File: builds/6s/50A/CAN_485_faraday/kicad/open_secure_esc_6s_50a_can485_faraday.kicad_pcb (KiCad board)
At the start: 4 copper layers, 32 x 66.1 mm, 59 parts, among them J1 SolderPad_1x04_SMD_P1.27mm_Pr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, J2 SolderPad_1x02_SMD_P2.54mm, J3 SolderPad_1x02_SMD_P2.54mm, J4A SolderWirePad_1x01_SMD_5x10mm, J4B SolderWirePad_1x01_SMD_5x10mm, J4C SolderWirePad_1x01_SMD_5x10mm, J5A SolderWire-6sqmm_1x01_D3.5mm_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, J5B SolderWire-6sqmm_1x01_D3.5mm_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, Q1 Toshiba_2-5W1A_SOP-Advance-N_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, Q2 Toshiba_2-5W1A_SOP-Advance-N_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, Q3 Toshiba_2-5W1A_SOP-Advance-N_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, Q4 Toshiba_2-5W1A_SOP-Advance-N_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, Q5 Toshiba_2-5W1A_SOP-Advance-N_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, Q6 Toshiba_2-5W1A_SOP-Advance-N_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, U1 LQFP-64_10x10mm_P0.5mm, U2 Infineon_PG-USON-10-2-4_3x3mm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, U3 SOIC-20W_7.5x12.8mm_P1.27mm, U4 SOIC-20W_7.5x12.8mm_P1.27mm, U5 TI_RTA0040B_WQFN-40_6x6mm_P0.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, U6 SOIC-8_3.9x4.9mm_P1.27mm, U7 SOIC-8_3.9x4.9mm_P1.27mm, U8 SOIC-8_3.9x4.9mm_P1.27mm

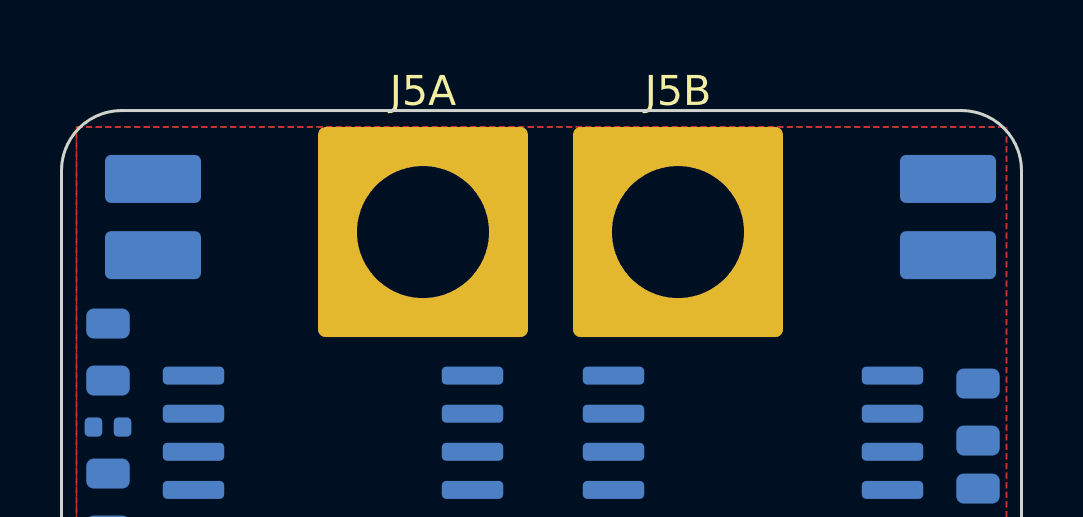
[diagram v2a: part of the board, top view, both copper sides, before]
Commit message: Check the PCB skills for IPC-2152: neither has it, and one misattributes 2221
The repo owner pointed at pcb-engineer and pcb-designer as holding IPC-2152
reference tables. Read both. Neither does.

pcb-engineer/references/design-rules.md prints

    Area = (I / (k x dT^0.44))^(1/0.725),  k = 0.048 external / 0.024 internal

under the heading "the IPC-2152 formula". Those are IPC-2221 Appendix A
constants, inherited from IPC-D-275. IPC-2152 replaced those curves BECAUSE
they were found inaccurate, and it publishes charts rather than a closed-form
k/b/c. conductor_sizing.py already recorded this in August; this run
quantifies it.

The document also disagrees with itself, and the error grows with current:

     I (A)   its table   its formula   ratio
       0.5        0.13          0.12   1.13x
       1.0        0.38          0.30   1.27x
       5.0        5.00          2.77   1.81x
      10.0       16.00          7.19   2.22x

This build runs at 50 A -- five times past that table's last row, in the
direction where its self-disagreement is worst.

pcb-designer carries no 2152 chart data at all; its trace table ends at
"Power >1A -> copper pour" and is silent at this current. Neither reference
carries a wire ampacity or AWG table, so neither speaks to the pack-lead
sizing flagged UNVERIFIED earlier -- IPC-2152 governs PCB conductors, not
wires, so it would not have anyway.

WHAT RUNNING IT ANYWAY REVEALS, recorded as information not citation: that
2221 equation asks for 14.28 mm (40 C rise) to 33.12 mm (10 C rise) of
external 2 oz conductor at 50 A. This build's phase pours are 7.50 mm -- two
to four times narrower.

That is not proof they are wrong. The equation models an isolated trace in
still air; these pours are 2.93 squares, wide, and pressed against the In1/In2
planes, and [47] measures a shipping 6S/50 A ESC at 103 C on a smaller board.
But it sizes the gap this design carries on unquantified plane spreading, and
it is precisely what IPC-2152's charts exist to s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
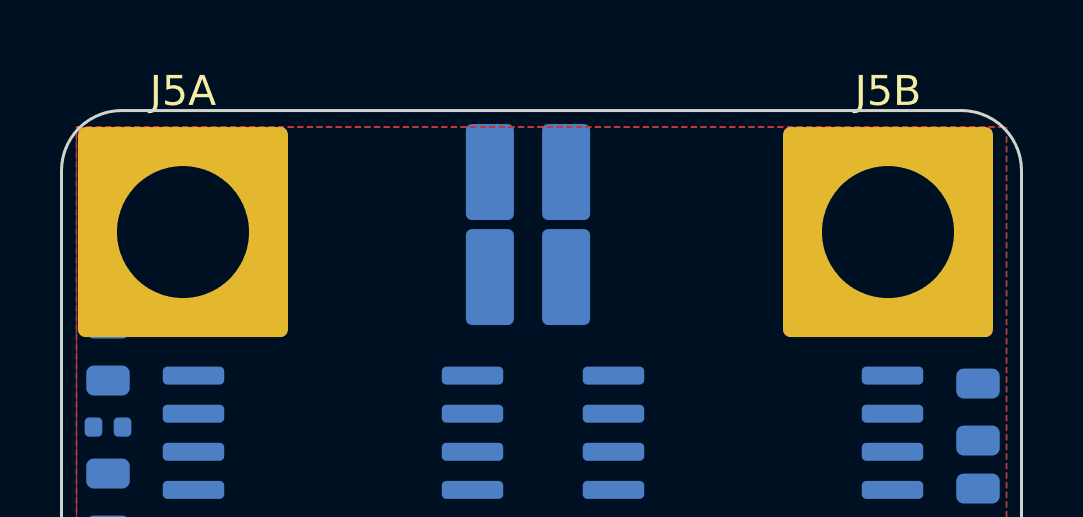
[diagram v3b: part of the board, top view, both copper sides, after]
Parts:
- moved J3 14.1 mm to (35.5, 25.5), turned to 180 degrees
- moved J2 12.6 mm to (35.5, 22.0), turned to 0 degrees
- moved J5A 8.00 mm to (24.0, 24.0)
- moved J5B 7.00 mm to (47.5, 24.0)
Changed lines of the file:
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@@
 	(footprint "SolderWire-6sqmm_1x01_D3.5mm_OD7mm"
 		(layer "F.Cu")
-		(at 32 24)
+		(at 24 24)
 		(descr "Soldered wire connection, for a single 6 mm² wire, reinforced insulation, conductor diameter 3.5mm, outer diameter 7mm, size source Multi-Contact FLEXI-xV 2.5 (https://www.staubli.com/content/dam/ecs/catalogs-brochures/TM/CAB-Main-11014119-en.pdf#page=11), bend radius 3 times outer diameter, generated with kicad-footprint-generator")
 		(tags "connector wire 6sqmm")
@@
 	(footprint "SolderWire-6sqmm_1x01_D3.5mm_OD7mm"
 		(layer "F.Cu")
-		(at 40.5 24)
+		(at 47.5 24)
 		(descr "Soldered wire connection, for a single 6 mm² wire, reinforced insulation, conductor diameter 3.5mm, outer diameter 7mm, size source Multi-Contact FLEXI-xV 2.5 (https://www.staubli.com/content/dam/ecs/catalogs-brochures/TM/CAB-Main-11014119-en.pdf#page=11), bend radius 3 times outer diameter, generated with kicad-footprint-generator")
 		(tags "connector wire 6sqmm")
@@
 	(footprint "SolderPad_1x02_SMD_P2.54mm"
 		(layer "B.Cu")
-		(at 23 23.5 90)
+		(at 35.5 22)
 		(descr "Bare SMD solder-pad strip, 2 pads, 2.54 mm pitch, 1.6 x 3.2 mm pads. Replaces a through-hole pin header so the opposite board side stays usable -- see symbols/tools/gen_smd_solder_pad_footprints.py. No connector body, no retention, no mating part: a wire solders directly to the pad. Pad geometry is an ENGINEERING DEFAULT (AGENTS.md Sec.4), not a datasheet or IPC value. Precedent: Vimdrones ESC S50 [47] 'CAN Port Connector: Solder PAD'.")
 		(tags "solder pad SMD wire connector 1x02 2.54mm")
 		(property "Reference" "J2"
-			(at 0 2.6 90)
+			(at 0 2.6 0)
 			(layer "B.SilkS")
 			(effects
@@
 		)
 		(property "Value" "SolderPad_1x02_SMD_P2.54mm"
-			(at 0 -2.6 90)
+			(at 0 -2.6 0)
 			(layer "B.Fab")
 			(effects
@@
 		)
 		(property "Datasheet" ""
-			(at 0 0 90)
+			(at 0 0 0)
 			(layer "B.Fab")
 			(hide yes)
@@
 		)
 		(property "Description" ""
-			(at 0 0 90)
+			(at 0 0 0)
 			(layer "B.Fab")
 			(hide yes)
@@
 		(attr smd)
 		(fp_line
-			(start 2.32 -1.85)
-			(end -2.32 -1.85)
+			(start -2.32 -1.85)
+			(end -2.32 1.85)
 			(stroke
 				(width 0.12)
@@
 		)
 		(fp_line
-			(start -2.32 -1.85)
-			(end -2.32 1.85)
+			(start -2.32 1.85)
+			(end 2.32 1.85)
 			(stroke
 				(width 0.12)
@@
 		)
 		(fp_line
-			(start 2.32 1.85)
-			(end 2.32 -1.85)
+			(start 2.32 -1.85)
+			(end -2.32 -1.85)
 			(stroke
 				(width 0.12)
@@
 		)
 		(fp_line
-			(start -2.32 1.85)
-			(end 2.32 1.85)
+			(start 2.32 1.85)
+			(end 2.32 -1.85)
 			(stroke
 				(width 0.12)
@@
 		)
 		(fp_line
-			(start 2.32 -1.85)
-			(end -2.32 -1.85)
+			(start -2.32 -1.85)
+			(end -2.32 1.85)
 			(stroke
 				(width 0.05)
@@
 		)
 		(fp_line
-			(start -2.32 -1.85)
-			(end -2.32 1.85)
+			(start -2.32 1.85)
+			(end 2.32 1.85)
 			(stroke
 				(width 0.05)
@@
 		)
 		(fp_line
-			(start 2.32 1.85)
-			(end 2.32 -1.85)
+			(start 2.32 -1.85)
+			(end -2.32 -1.85)
 			(stroke
 				(width 0.05)
@@
 		)
 		(fp_line
-			(start -2.32 1.85)
-			(end 2.32 1.85)
+			(start 2.32 1.85)
+			(end 2.32 -1.85)
 			(stroke
 				(width 0.05)
@@
 		)
 		(fp_text user "${REFERENCE}"
-			(at 0 0 90)
+			(at 0 0 0)
 			(layer "B.Fab")
 			(effects
@@
 		)
 		(pad "1" smd roundrect
-			(at -1.27 0 90)
+			(at -1.27 0)
 			(size 1.6 3.2)
 			(layers "B.Cu" "B.Mask" "B.Paste")
@@
 		)
 		(pad "2" smd roundrect
-			(at 1.27 0 90)
+			(at 1.27 0)
 			(size 1.6 3.2)
 			(layers "B.Cu" "B.Mask" "B.Paste")
@@
 	(footprint "SolderPad_1x02_SMD_P2.54mm"
 		(layer "B.Cu")
-		(at 49.5 23.5 -90)
+		(at 35.5 25.5 180)
 		(descr "Bare SMD solder-pad strip, 2 pads, 2.54 mm pitch, 1.6 x 3.2 mm pads. Replaces a through-hole pin header so the opposite board side stays usable -- see symbols/tools/gen_smd_solder_pad_footprints.py. No connector body, no retention, no mating part: a wire solders directly to the pad. Pad geometry is an ENGINEERING DEFAULT (AGENTS.md Sec.4), not a datasheet or IPC value. Precedent: Vimdrones ESC S50 [47] 'CAN Port Connector: Solder PAD'.")
 		(tags "solder pad SMD wire connector 1x02 2.54mm")
 		(property "Reference" "J3"
-			(at 0 2.6 90)
+			(at 0 2.6 0)
 			(layer "B.SilkS")
 			(effects
@@
 		)
 		(property "Value" "SolderPad_1x02_SMD_P2.54mm"
-			(at 0 -2.6 90)
+			(at 0 -2.6 0)
 			(layer "B.Fab")
 			(effects
@@
 		)
 		(property "Datasheet" ""
-			(at 0 0 90)
+			(at 0 0 0)
 			(layer "B.Fab")
 			(hide yes)
@@
 		)
 		(property "Description" ""
-			(at 0 0 90)
+			(at 0 0 0)
 			(layer "B.Fab")
 			(hide yes)
@@
 		(attr smd)
 		(fp_line
-			(start -2.32 1.85)
-			(end 2.32 1.85)
+			(start 2.32 1.85)
+			(end 2.32 -1.85)
 			(stroke
 				(width 0.12)
@@
 		)
 		(fp_line
-			(start 2.32 1.85)
-			(end 2.32 -1.85)
+			(start 2.32 -1.85)
+			(end -2.32 -1.85)
 			(stroke
 				(width 0.12)
@@
 		)
 		(fp_line
-			(start -2.32 -1.85)
-			(end -2.32 1.85)
+			(start -2.32 1.85)
+			(end 2.32 1.85)
 			(stroke
 				(width 0.12)
@@
 		)
 		(fp_line
-			(start 2.32 -1.85)
-			(end -2.32 -1.85)
+			(start -2.32 -1.85)
+			(end -2.32 1.85)
 			(stroke
 				(width 0.12)
@@
 		)
 		(fp_line
-			(start -2.32 1.85)
-			(end 2.32 1.85)
+			(start 2.32 1.85)
+			(end 2.32 -1.85)
 			(stroke
 				(width 0.05)
@@
 		)
 		(fp_line
-			(start 2.32 1.85)
-			(end 2.32 -1.85)
+			(start 2.32 -1.85)
+			(end -2.32 -1.85)
 			(stroke
 				(width 0.05)
@@
 		)
 		(fp_line
-			(start -2.32 -1.85)
-			(end -2.32 1.85)
+			(start -2.32 1.85)
+			(end 2.32 1.85)
 			(stroke
 				(width 0.05)
@@
 		)
 		(fp_line
-			(start 2.32 -1.85)
-			(end -2.32 -1.85)
+			(start -2.32 -1.85)
+			(end -2.32 1.85)
 			(stroke
 				(width 0.05)
@@
 		)
 		(fp_text user "${REFERENCE}"
-			(at 0 0 90)
+			(at 0 0 0)
 			(layer "B.Fab")
 			(effects
@@
 		)
 		(pad "1" smd roundrect
-			(at -1.27 0 270)
+			(at -1.27 0 180)
 			(size 1.6 3.2)
 			(layers "B.Cu" "B.Mask" "B.Paste")
@@
 		)
 		(pad "2" smd roundrect
-			(at 1.27 0 270)
+			(at 1.27 0 180)
 			(size 1.6 3.2)
 			(layers "B.Cu" "B.Mask" "B.Paste")

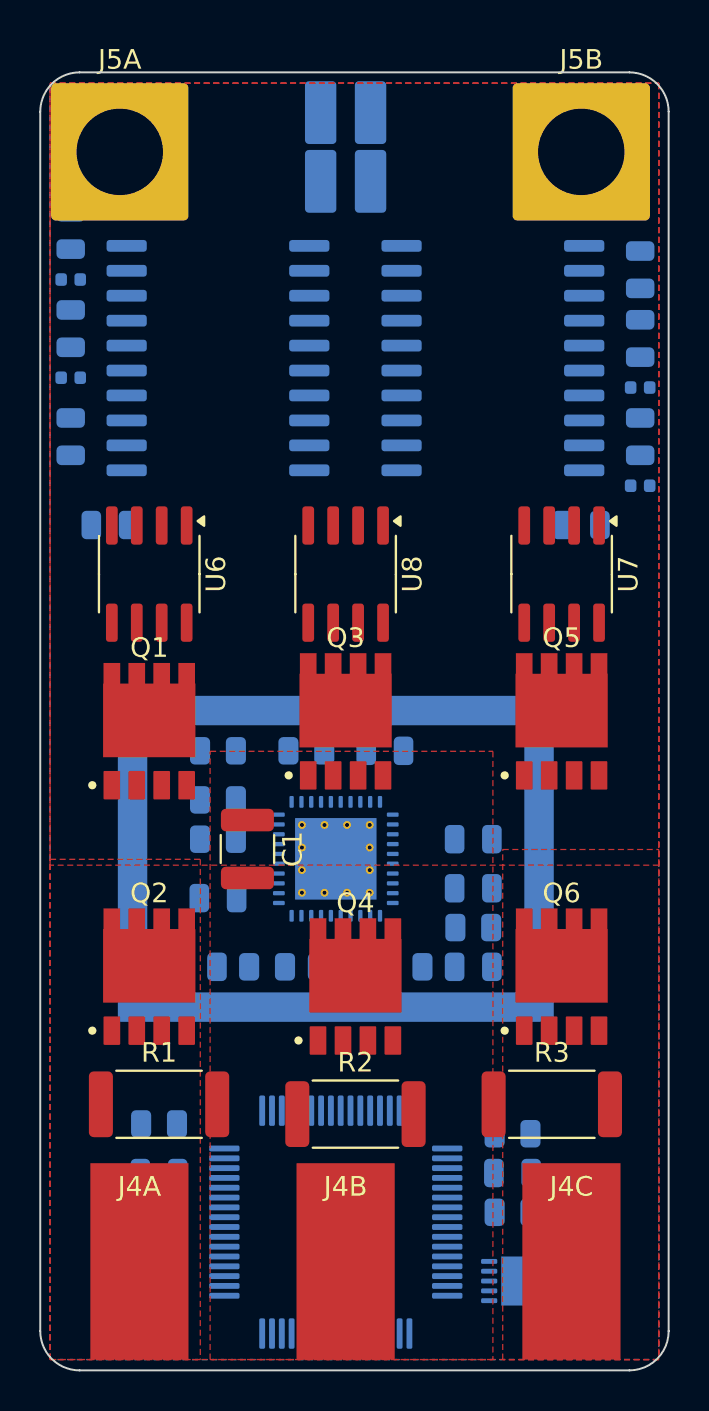
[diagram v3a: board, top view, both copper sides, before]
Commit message: Creepage PASSES at 7.51 mm -- the owner's 90-degree rotation was the answer
First time this session the 7.5 mm requirement of [9] Table 6 is met, measured
edge-to-edge with the around-the-edge path included.

    creepage min      2.80 -> 7.51 mm   PASSES
    isolated lead max         9.16 mm   (limit 10)
    gate loop max            16.49 mm
    DRC electrical                  2   (two courtyard overlaps, below)

TWO IDEAS FROM THE OWNER, BOTH RIGHT, AND THE SECOND IS WHAT DID IT.

Option B -- pack terminals SMD on F.Cu only -- works because creepage is a
SURFACE measure and every isolated part sits on B.Cu. It took creepage
2.80 -> 4.64 and removed the pack as a same-layer offender entirely. It needed
the F.Cu VM/GND pours notched to x 5.12..26.88 for the depth of the isolated
section, because the around-the-edge path (F.Cu inset + 1.6 mm board + B.Cu
inset) was only 2.93 mm with a full-width pour.

Then rotating U3 by -90 and U4 by +90, isolated rows facing the board end,
took it 4.64 -> 7.51. The reason is precise: the support columns used to sit
0.72-0.82 mm from the side edges, so anything opposite them anywhere on the
board needed a 5.08 mm inset. With the ICs themselves outboard at ~2.94 mm,
that requirement drops to 2.96 mm -- a 2.1 mm relaxation on both edges, which
is what had been defeating every previous fix.

MY FIRST TEST OF THAT ROTATION WAS UNFAIR AND I SAID SO. Rotating the support
parts rigidly about each IC centre swung them from beside the IC to above and
below it; C12 ended 17 mm from the pin it serves, creepage read 0.00 and DRC
19. Those were artifacts of the transform, not of the arrangement. Re-placed
by pin position instead -- each part above the pins it bridges -- the same
rotation gives 7.51 mm.

HARNESS EXTENDED, AND THIS MATTERED. score_placement.py now measures the
around-the-edge creepage path for pairs that share no copper layer:

    path = insetA + board thickness + insetB, minimised over the four edges

Without it, option B would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
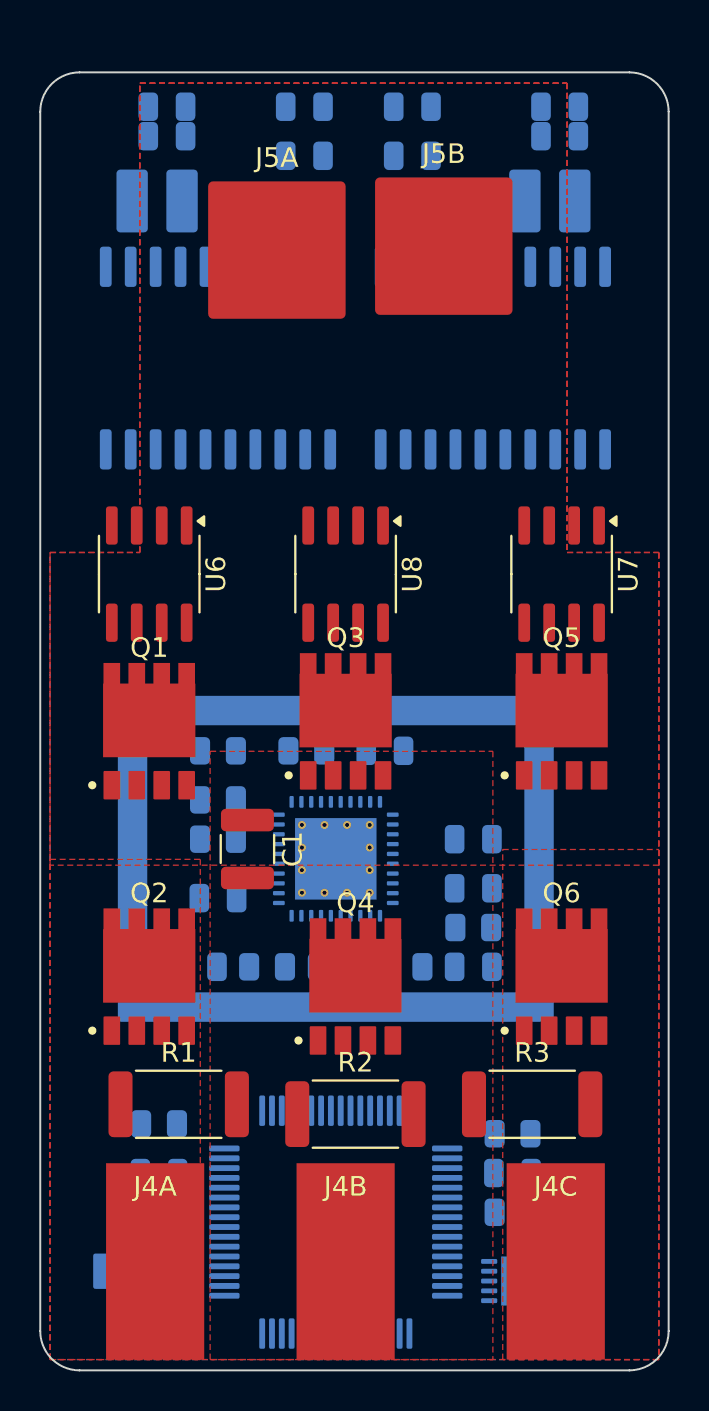
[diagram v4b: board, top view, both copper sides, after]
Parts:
- moved C14 20.0 mm to (26.4, 23.2)
- moved C18 19.8 mm to (46.4, 23.2)
- moved C13 17.5 mm to (26.4, 21.7), turned to 0 degrees
- moved C17 17.3 mm to (46.4, 21.7), turned to 0 degrees
- moved FB4 17.1 mm to (41.4, 26.5)
- moved C11 16.4 mm to (33.4, 21.7), turned to 0 degrees
- moved FB3 15.0 mm to (38.9, 26.5)
- moved C16 14.9 mm to (38.9, 24.2), turned to 0 degrees
- moved C15 14.3 mm to (38.9, 21.7), turned to 0 degrees
- moved FB2 12.7 mm to (30.4, 26.5), turned to 0 degrees
- moved C12 12.5 mm to (33.4, 24.2), turned to 0 degrees
- moved FB1 12.1 mm to (32.9, 26.5), turned to 0 degrees
- moved J2 10.6 mm to (25.9, 26.5)
- moved J3 10.4 mm to (45.9, 26.5), turned to 0 degrees
- moved J5A 9.43 mm to (32.0, 29.0)
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
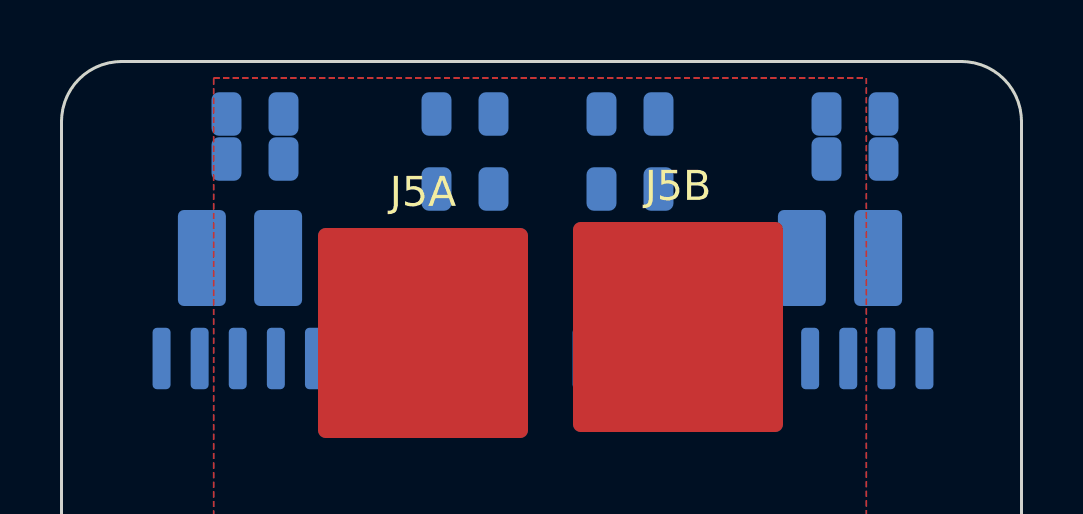
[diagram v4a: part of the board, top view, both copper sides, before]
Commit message: Clear the last two courtyard overlaps: creepage 7.51, DRC electrical 0
C13/C14 and C17/C18 were not stacked as I had assumed from the bounding box --
their footprints define no courtyard, so my helper had been falling back to
GetBoundingBox, which includes silkscreen and made both pairs read as
identically placed. Measured from pads they sit side by side with a 1.55 mm
gap, and it was DRC's own implied courtyard that overlapped.

Widened both pairs. C13 moved +1.5 mm toward U3.16, the pin it serves, so the
separation and its lead length improve together; C17 moved -1.5 mm away from
C18. That cleared both overlaps but cost 0.09 mm of creepage, which C18 -0.4 mm
recovered.

    creepage min       7.51 mm   PASS
    isolated lead max  9.76 mm   (limit 10)
    DRC electrical           0

AND THE MORE IMPORTANT RESULT: 7.51 IS A CEILING, NOT A MARGIN.

The binding pair is no longer anything nudgeable. It is U3.20 (CAN_GNDISO)
against U4.10 (GND) at 7.51 mm, in-plane, diagonally across the 1.97 mm
channel between the two packages. It grows only by separating the
transceivers, and they already span x 3.08..29.11 of a 30.90 mm usable width.

The two constraints now oppose each other: moving the ICs apart improves that
in-plane pair but shortens the around-the-edge paths, whose next binders sit
at 7.58-7.83 mm. 32 mm width is close to the balance point, so the board
passes by 0.01 mm and cannot do better at this width.

0.01 mm is not a manufacturing margin. It is smaller than fab registration
tolerance and fifty times smaller than the 0.5 mm grid the rest of the
placement is snapped to -- any later move, including a routine grid snap,
breaks it. Recorded as 12.5.al with an estimate of ~2 mm additional width for
a defensible ~8.5 mm, and referred back: accept the ceiling and freeze
placement, or widen to 34 mm.

Co-Authored-By: Claude Opus 5 <noreply@anthropic.com>
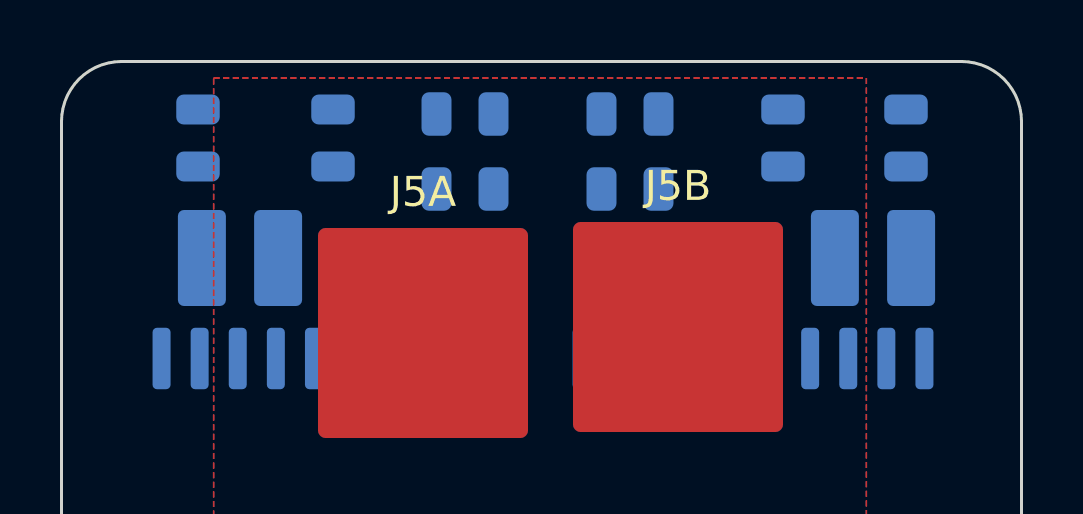
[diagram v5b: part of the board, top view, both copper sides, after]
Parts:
- moved C13 2.72 mm to (29.0, 22.5), turned to -90 degrees
- moved C17 2.53 mm to (44.0, 22.5), turned to -90 degrees
- moved C14 2.02 mm to (24.5, 22.5), turned to -90 degrees
- moved C18 1.84 mm to (48.1, 22.5), turned to -90 degrees
- moved J3 1.10 mm to (47.0, 26.5)
